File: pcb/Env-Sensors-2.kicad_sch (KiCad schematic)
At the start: 16 parts, among them Q1 MMBFJ201, U10 TSL2591, U13 BMP581, U14 MCP6042, U15 ADS1115, U18 TGS5141

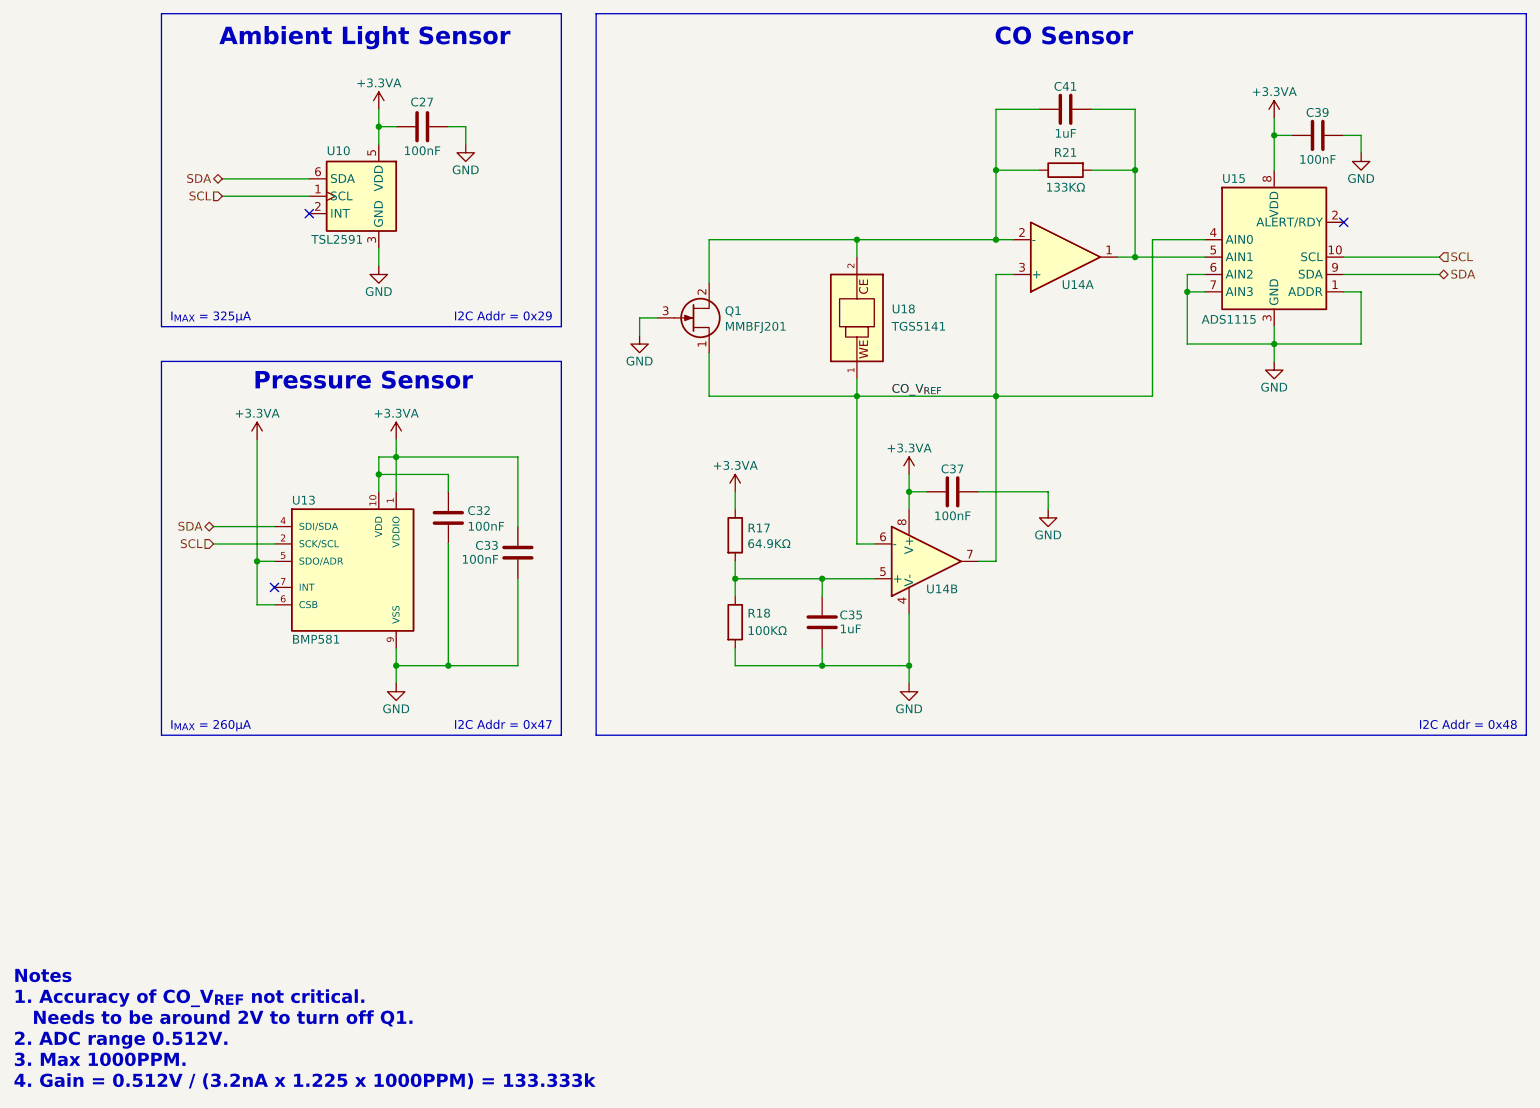
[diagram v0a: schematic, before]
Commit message: Minor changes
Separate SEN66 on a separate I2C bus.
Add WIFi Antenna cutout.
Beef-up Power and Ground connections to SEN66.
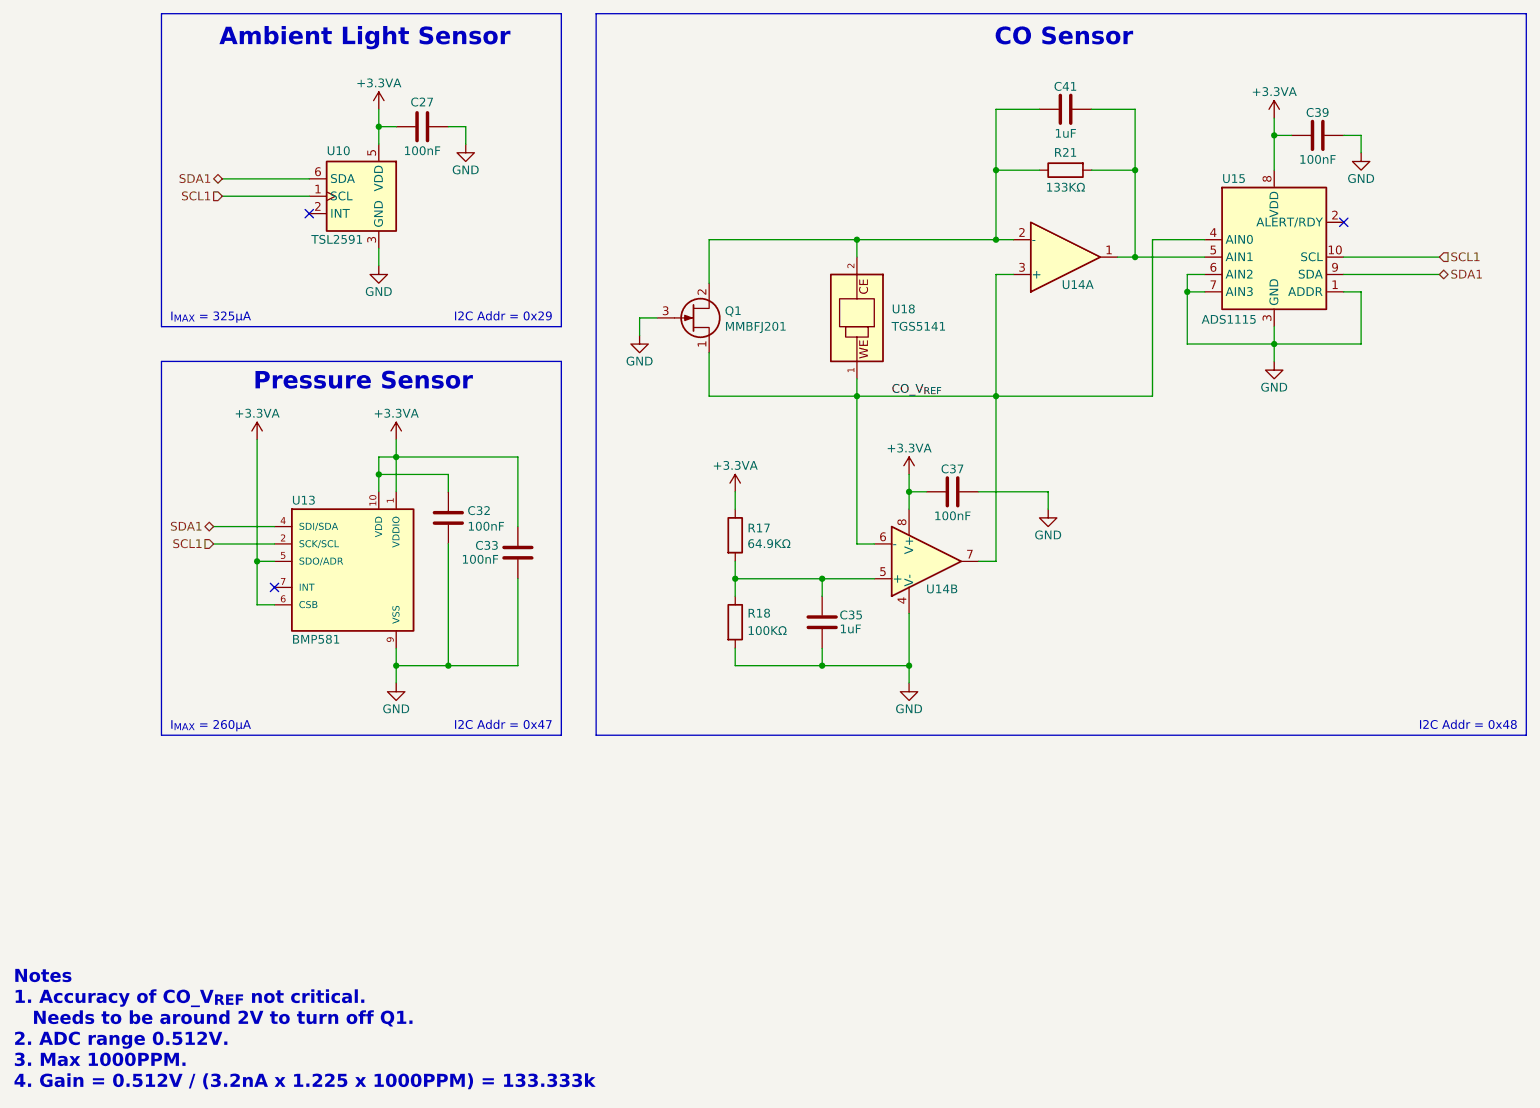
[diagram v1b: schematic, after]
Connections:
- net SCL renamed SCL1
- net SDA renamed SDA1
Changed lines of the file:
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@@
 	(title_block
 		(title "ESPHome Parking Assistant")
-		(date "2025-04-10")
-		(rev "-")
+		(date "2025-04-18")
+		(rev "A")
 		(company "Mike Lawrence")
 	)
@@
 		)
 	)
-	(hierarchical_label "SDA"
+	(hierarchical_label "SDA1"
 		(shape bidirectional)
 		(at 54.61 100.33 180)
@@
 		)
 	)
-	(hierarchical_label "SCL"
+	(hierarchical_label "SCL1"
 		(shape input)
 		(at 54.61 102.87 180)
@@
 		)
 	)
-	(hierarchical_label "SCL"
+	(hierarchical_label "SCL1"
 		(shape input)
 		(at 233.68 60.96 0)
@@
 		)
 	)
-	(hierarchical_label "SDA"
+	(hierarchical_label "SDA1"
 		(shape bidirectional)
 		(at 55.88 49.53 180)
@@
 		)
 	)
-	(hierarchical_label "SCL"
+	(hierarchical_label "SCL1"
 		(shape input)
 		(at 55.88 52.07 180)
@@
 		)
 	)
-	(hierarchical_label "SDA"
+	(hierarchical_label "SDA1"
 		(shape bidirectional)
 		(at 233.68 63.5 0)
